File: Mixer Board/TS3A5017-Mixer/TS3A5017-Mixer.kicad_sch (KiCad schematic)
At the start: 10 parts, among them J1 RF-In, J2 CLK0, J3 CLK1, J4 Conn_01x06, U1 TS3A5017RGY

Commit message: Finish first iteration, generate manufacturing files
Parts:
- J1, J2, J3: footprint Connector_Coaxial:SMA_Amphenol_901-143_Horizontal -> Connector_Amphenol:AMPHENOL_901-143-6RFX
- J4: footprint (none) -> Connector_PinHeader_2.54mm:PinHeader_1x06_P2.54mm_Vertical
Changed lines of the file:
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@@
 			)
 		)
-		(property "Footprint" ""
+		(property "Footprint" "Connector_PinHeader_2.54mm:PinHeader_1x06_P2.54mm_Vertical"
 			(at 189.23 97.79 0)
 			(effects
@@
 			)
 		)
-		(property "Footprint" "Connector_Coaxial:SMA_Amphenol_901-143_Horizontal"
+		(property "Footprint" "Connector_Amphenol:AMPHENOL_901-143-6RFX"
 			(at 85.09 96.52 0)
 			(effects
@@
 			)
 		)
-		(property "Footprint" "Connector_Coaxial:SMA_Amphenol_901-143_Horizontal"
+		(property "Footprint" "Connector_Amphenol:AMPHENOL_901-143-6RFX"
 			(at 85.09 106.68 0)
 			(effects
@@
 			)
 		)
-		(property "Footprint" "Connector_Coaxial:SMA_Amphenol_901-143_Horizontal"
+		(property "Footprint" "Connector_Amphenol:AMPHENOL_901-143-6RFX"
 			(at 85.09 116.84 0)
 			(effects

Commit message: Working on mixer board
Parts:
- removed J4: Conn_01x06, Connector_PinHeader_2.54mm:PinHeader_1x06_P2.54mm_Vertical, symbol Connector_Generic:Conn_01x06
- added C10, C11, C12, C13, C6, C7, C8, C9: .1uf, Capacitor_SMD:C_0201_0603Metric, symbol Device:C_Small
- added J4: AudioJack4_Ground, Connector_Audio:Jack_3.5mm_CUI_SJ-3523-SMT_Horizontal, symbol Connector_Audio:AudioJack4_Ground
- added R1, R2: 10k, Resistor_SMD:R_0201_0603Metric, symbol Device:R_US
- added U2, U3: LMP7715MF, Package_TO_SOT_SMD:SOT-23-5, symbol Amplifier_Operational:LMP7715MF
- J1, J2, J3: footprint Connector_Amphenol:AMPHENOL_901-143-6RFX -> Connector_Coaxial:SMA_Amphenol_901-143_Horizontal
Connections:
- net 3.3V: now also C10.2, C6.2, U2.5 (V+), U3.5 (V+)
- net GND: now also C10.1, C11.1, C12.1, C6.1, C8.1, C9.1, J4.R2, J4.S, U2.2 (V-), U3.2 (V-)
- new net: C12.2, C13.2, R2.1, U3.4 (IN-)
- new net: C7.1, J4.R1, R1.2, U2.1 (OUT)
- new net: C13.1, J4.T, R2.2, U3.1 (OUT)
- new net: C7.2, C8.2, R1.1, U2.4 (IN-)
- new net: C9.2, U2.3 (IN+)
- new net: C11.2, U3.3 (IN+)

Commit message: Workig on mixer board
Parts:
- C2, C3, C4, C5: footprint Capacitor_SMD:C_1206_3216Metric -> Capacitor_SMD:C_0201_0603Metric
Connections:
- net I-Neg: now reaches C12.2, C13.2, R2.1, U3.4 (IN-)
- net I-Neg: now also C2.1, U1.13 (2S4), U1.3 (1S4)
- net Q-Neg: now reaches C7.2, C8.2, R1.1, U2.4 (IN-)
- net Q-Neg: now also C3.1, U1.12 (2S3), U1.4 (1S3)
- net Q-Pos: now reaches C9.2, U2.3 (IN+)
- net Q-Pos: now also C5.1, U1.10 (2S1), U1.6 (1S1)
- net I-Pos: now reaches C11.2, U3.3 (IN+)
- net I-Pos: now also C4.1, U1.11 (2S2), U1.5 (1S2)
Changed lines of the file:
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@@
+		)
+	)
+	(label "Q-Neg"
+		(at 179.07 100.33 0)
+		(fields_autoplaced yes)
+		(effects
+			(font
+				(size 1.27 1.27)
+			)
+			(justify left bottom)
+		)
+	)
+	(label "I-Neg"
+		(at 179.07 102.87 0)
+		(fields_autoplaced yes)
+		(effects
+			(font
+				(size 1.27 1.27)
+			)
+			(justify left bottom)
+		)
+	)
+	(label "Q-Pos"
+		(at 179.07 95.25 0)
+		(fields_autoplaced yes)
+		(effects
+			(font
+				(size 1.27 1.27)
+			)
+			(justify left bottom)
+		)
+	)
+	(label "Q-Pos"
+		(at 203.2 63.5 180)
+		(fields_autoplaced yes)
+		(effects
+			(font
+				(size 1.27 1.27)
+			)
+			(justify right bottom)
+		)
+	)
+	(label "Q-Neg"
+		(at 204.47 85.09 180)
+		(fields_autoplaced yes)
+		(effects
+			(font
+				(size 1.27 1.27)
+			)
+			(justify right bottom)
+		)
+	)
+	(label "I-Pos"
+		(at 204.47 114.3 0)
+		(fields_autoplaced yes)
+		(effects
+			(font
+				(size 1.27 1.27)
+			)
+			(justify left bottom)
+		)
+	)
+	(label "I-Neg"
+		(at 203.2 135.89 180)
+		(fields_autoplaced yes)
+		(effects
+			(font
+				(size 1.27 1.27)
+			)
+			(justify right bottom)
+		)
+	)
+	(label "I-Pos"
+		(at 179.07 97.79 0)
+		(fields_autoplaced yes)
+		(effects
+			(font
+				(size 1.27 1.27)
+			)
+			(justify left bottom)
 		)
 	)
@@
 		)
 	)
-	(netclass_flag ""
-		(length 2.54)
-		(shape round)
-		(at 203.2 114.3 90)
-		(effects
-			(font
-				(size 1.27 1.27)
-			)
-			(justify left bottom)
-		)
-		(property "Netclass" "I-Pos"
-			(at 199.39 114.3 0)
-			(effects
-				(font
-					(size 1.27 1.27)
-					(italic yes)
-				)
-				(justify right)
-			)
-		)
-	)
-	(netclass_flag ""
-		(length 2.54)
-		(shape round)
-		(at 184.15 97.79 270)
-		(effects
-			(font
-				(size 1.27 1.27)
-			)
-			(justify right bottom)
-		)
-		(property "Netclass" "I-Pos"
-			(at 187.96 97.79 0)
-			(effects
-				(font
-					(size 1.27 1.27)
-					(italic yes)
-				)
-				(justify left)
-			)
-		)
-	)
-	(netclass_flag ""
-		(length 2.54)
-		(shape round)
-		(at 184.15 100.33 270)
-		(effects
-			(font
-				(size 1.27 1.27)
-			)
-			(justify right bottom)
-		)
-		(property "Netclass" "Q-Neg"
-			(at 187.96 100.33 0)
-			(effects
-				(font
-					(size 1.27 1.27)
-					(italic yes)
-				)
-				(justify left)
-			)
-		)
-	)
-	(netclass_flag ""
-		(length 2.54)
-		(shape round)
-		(at 203.2 135.89 90)
-		(effects
-			(font
-				(size 1.27 1.27)
-			)
-			(justify left bottom)
-		)
-		(property "Netclass" "I-Neg"
-			(at 199.39 135.89 0)
-			(effects
-				(font
-					(size 1.27 1.27)
-					(italic yes)
-				)
-				(justify right)
-			)
-		)
-	)
-	(netclass_flag ""
-		(length 2.54)
-		(shape round)
-		(at 184.15 95.25 270)
-		(effects
-			(font
-				(size 1.27 1.27)
-			)
-			(justify right bottom)
-		)
-		(property "Netclass" "Q-Pos"
-			(at 187.96 95.25 0)
-			(effects
-				(font
-					(size 1.27 1.27)
-					(italic yes)
-				)
-				(justify left)
-			)
-		)
-	)
-	(netclass_flag ""
-		(length 2.54)
-		(shape round)
-		(at 184.15 102.87 270)
-		(effects
-			(font
-				(size 1.27 1.27)
-			)
-			(justify right bottom)
-		)
-		(property "Netclass" "I-Neg"
-			(at 187.96 102.87 0)
-			(effects
-				(font
-					(size 1.27 1.27)
-					(italic yes)
-				)
-				(justify left)
-			)
-		)
-	)
-	(netclass_flag ""
-		(length 2.54)
-		(shape round)
-		(at 203.2 63.5 90)
-		(effects
-			(font
-				(size 1.27 1.27)
-			)
-			(justify left bottom)
-		)
-		(property "Netclass" "Q-Pos"
-			(at 199.39 63.5 0)
-			(effects
-				(font
-					(size 1.27 1.27)
-					(italic yes)
-				)
-				(justify right)
-			)
-		)
-	)
-	(netclass_flag ""
-		(length 2.54)
-		(shape round)
-		(at 203.2 85.09 90)
-		(effects
-			(font
-				(size 1.27 1.27)
-			)
-			(justify left bottom)
-		)
-		(property "Netclass" "Q-Neg"
-			(at 199.39 85.09 0)
-			(effects
-				(font
-					(size 1.27 1.27)
-					(italic yes)
-				)
-				(justify right)
-			)
-		)
-	)
 	(symbol
 		(lib_id "Device:C_Small")
@@
 		(fields_autoplaced yes)
 		(property "Reference" "J4"
-			(at 281.94 97.1549 0)
+			(at 281.94 98.4249 0)
 			(effects
 				(font
@@
 				)
 				(justify right)
+				(hide yes)
 			)
 		)
@@
 			)
 		)
-		(property "Footprint" "Capacitor_SMD:C_1206_3216Metric"
+		(property "Footprint" "Capacitor_SMD:C_0201_0603Metric"
 			(at 163.83 106.68 0)
 			(effects
@@
 			)
 		)
-		(property "Footprint" "Capacitor_SMD:C_1206_3216Metric"
+		(property "Footprint" "Capacitor_SMD:C_0201_0603Metric"
 			(at 176.53 106.68 0)
 			(effects
@@
 			)
 		)
-		(property "Footprint" "Capacitor_SMD:C_1206_3216Metric"
+		(property "Footprint" "Capacitor_SMD:C_0201_0603Metric"
 			(at 157.48 106.68 0)
 			(effects
@@
 			)
 		)
-		(property "Footprint" "Capacitor_SMD:C_1206_3216Metric"
+		(property "Footprint" "Capacitor_SMD:C_0201_0603Metric"
 			(at 170.18 106.68 0)
 			(effects

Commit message: Working on stuff
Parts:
- removed J4: AudioJack4_Ground, Connector_Audio:Jack_3.5mm_CUI_SJ-3523-SMT_Horizontal, symbol Connector_Audio:AudioJack4_Ground
- added C14, C15: 1uf, Capacitor_SMD:C_0201_0603Metric, symbol Device:C_Small
- added J4: Conn_01x02_Pin, Connector_PinHeader_2.54mm:PinHeader_1x02_P2.54mm_Vertical, symbol Connector:Conn_01x02_Pin
- added J5: PJ-320D-A, Connector_Audio:HRO_PJ-320D-A, symbol Connector_Audio:PJ-320D-A
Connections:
- net 3.3V: now also J4.1 (Pin_1)
- net GND: now also J4.2 (Pin_2), J5.1, J5.3
- net at C7.1, R1.2, U2.1 (OUT): now also C15.1
- net at C13.1, R2.2, U3.1 (OUT): now also C14.2
- new net: C14.1, J5.4
- new net: C15.2, J5.2

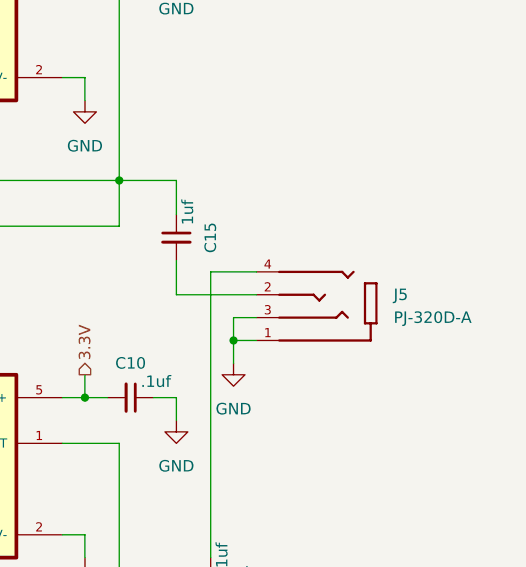
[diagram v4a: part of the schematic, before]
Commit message: Working on silkscreen and ordering
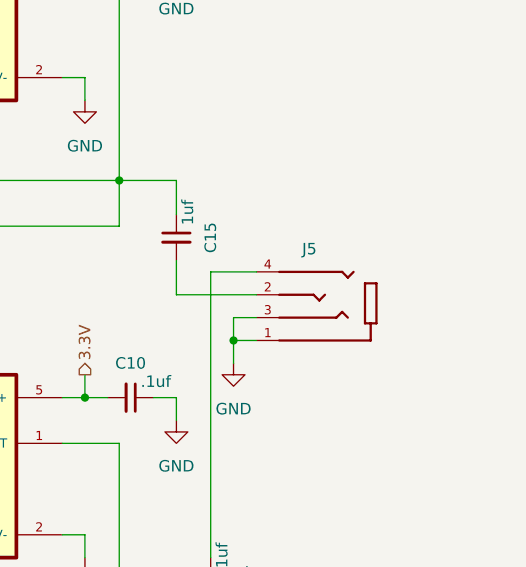
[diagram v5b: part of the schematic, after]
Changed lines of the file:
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@@
 		(on_board yes)
 		(dnp no)
-		(fields_autoplaced yes)
 		(property "Reference" "J5"
-			(at 283.21 97.7899 0)
+			(at 273.05 92.71 0)
 			(effects
 				(font
@@
 				)
 				(justify right)
+				(hide yes)
 			)
 		)

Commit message: Fixing things
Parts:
- C1: footprint Capacitor_SMD:C_0603_1608Metric -> Capacitor_SMD:C_0201_0603Metric
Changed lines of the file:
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@@
 			)
 		)
-		(property "Footprint" "Capacitor_SMD:C_0603_1608Metric"
+		(property "Footprint" "Capacitor_SMD:C_0201_0603Metric"
 			(at 119.38 80.01 0)
 			(effects
